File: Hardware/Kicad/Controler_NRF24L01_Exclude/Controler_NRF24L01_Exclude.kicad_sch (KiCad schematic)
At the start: 38 parts, among them J1 Conn_01x02, J2 Conn_02x07_Odd_Even, J3 Conn_01x03, J4 Conn_01x03, SW1 SW_Push, SW10 SW_Push, SW11 SW_DIP_x01, SW13 SW_DIP_x01, SW2 SW_Push, SW3 SW_Push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

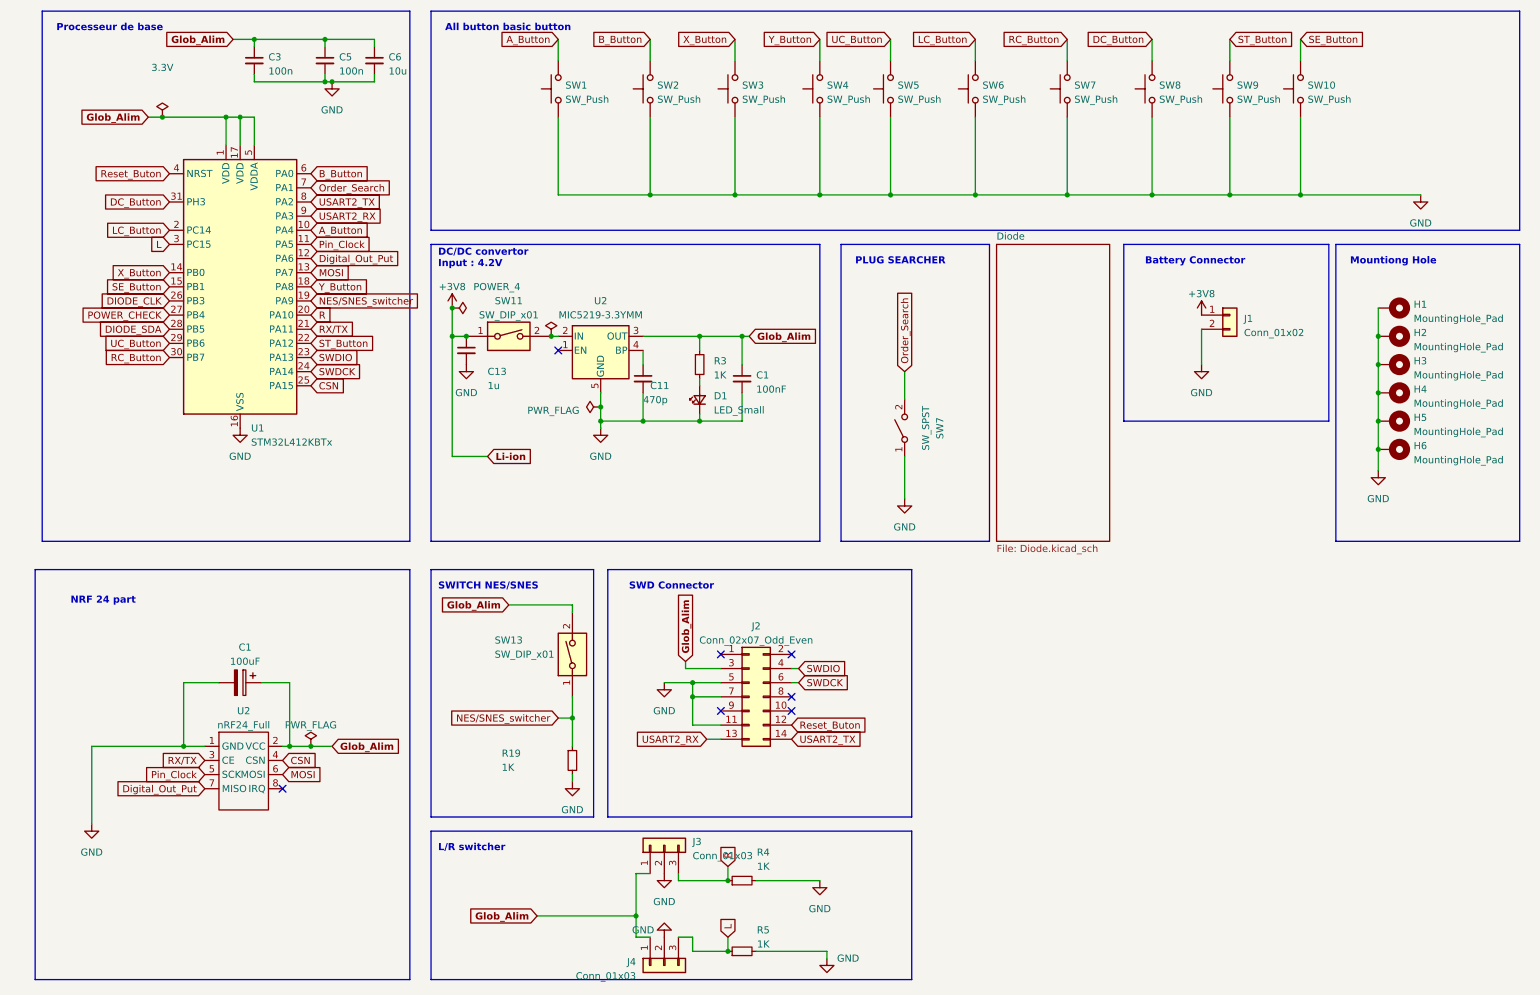
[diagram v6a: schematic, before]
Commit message: Update v2.2a - Plug_NRF24L01_Exclude (SWD_Connector, GND Vias) - Controller_NRF24L01_Exclude (Schematic) - Cleaned Folders
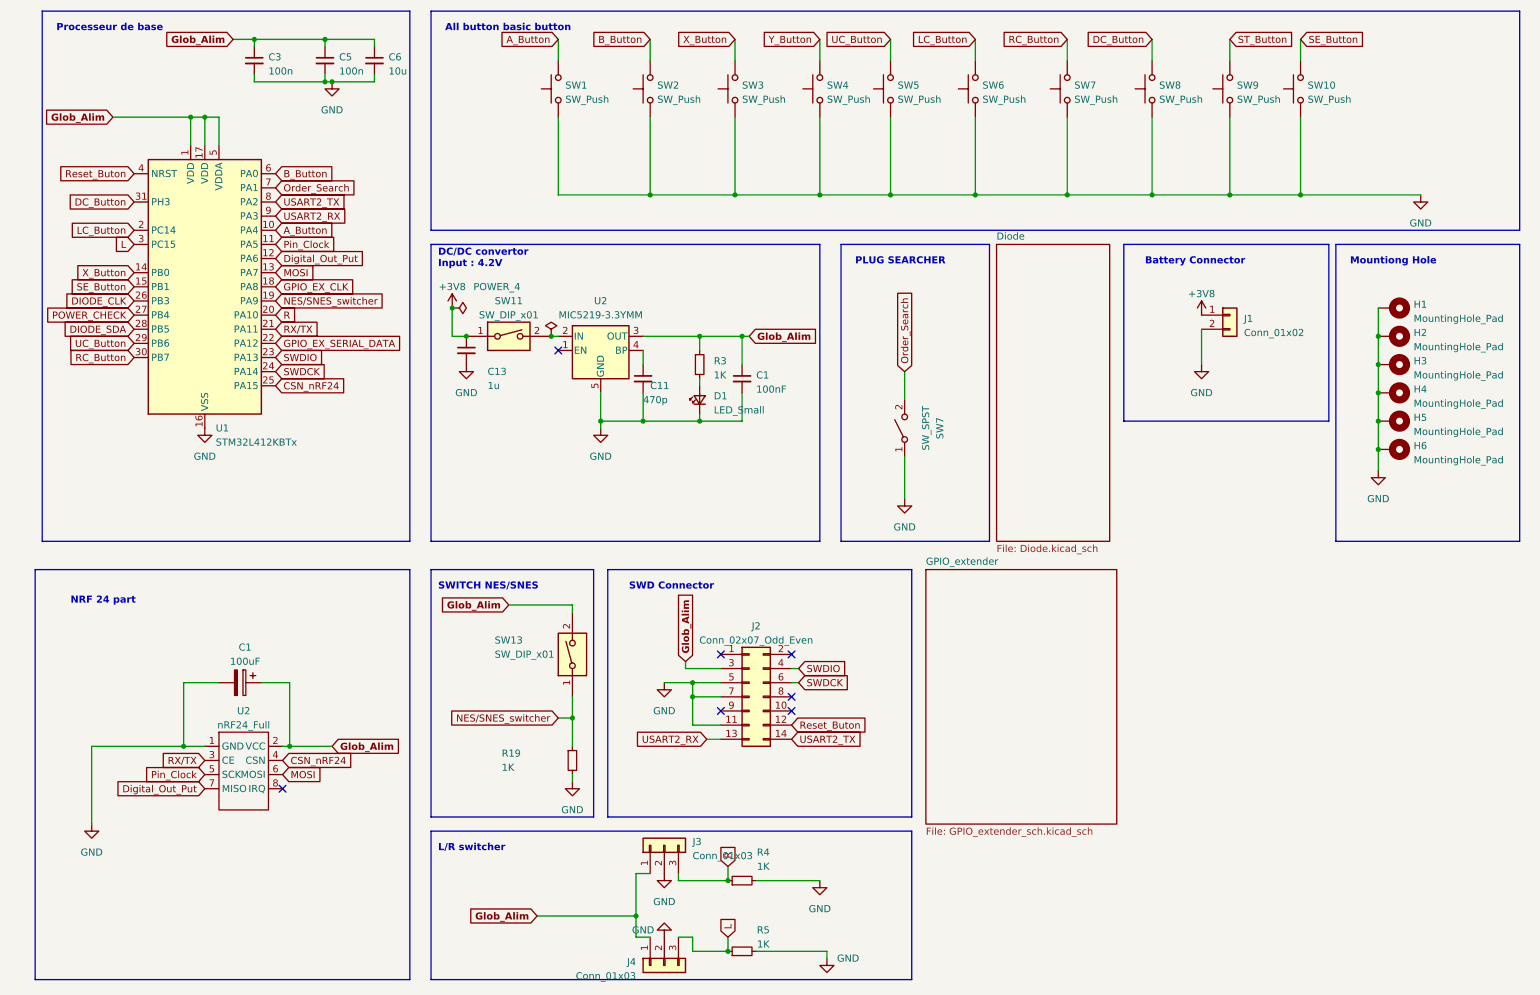
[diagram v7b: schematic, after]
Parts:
- C1: footprint Capacitor_SMD:CP_Elec_5x5.4 -> Capacitor_SMD:C_0603_1608Metric_Pad1.08x0.95mm_HandSolder
- C3, C5, C6: footprint Resistor_SMD:R_0603_1608Metric_Pad0.98x0.95mm_HandSolder -> Capacitor_SMD:C_0603_1608Metric_Pad1.08x0.95mm_HandSolder
- U2: footprint Connector_PinHeader_2.00mm:PinHeader_2x04_P2.00mm_Vertical -> Connector_PinHeader_2.54mm:PinHeader_2x04_P2.54mm_Vertical
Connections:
- net ST_Button: no longer U1.22 (PA12)
- net Y_Button: no longer U1.18 (PA8)
- net CSN renamed CSN_nRF24
- new net GPIO_EX_CLK: U1.18 (PA8)
- new net GPIO_EX_SERIAL_DATA: U1.22 (PA12)
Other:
- added sheet GPIO_extender (GPIO_extender_sch.kicad_sch)
- moved on the sheet: U1
